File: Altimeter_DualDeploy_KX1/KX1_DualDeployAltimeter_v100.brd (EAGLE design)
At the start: 48.3 x 50.8 mm, 44 parts, among them J1 AVR_SPI_PRG_6NS, U1 ATMEGA328P, U2 BMP180, Y3 16MHz

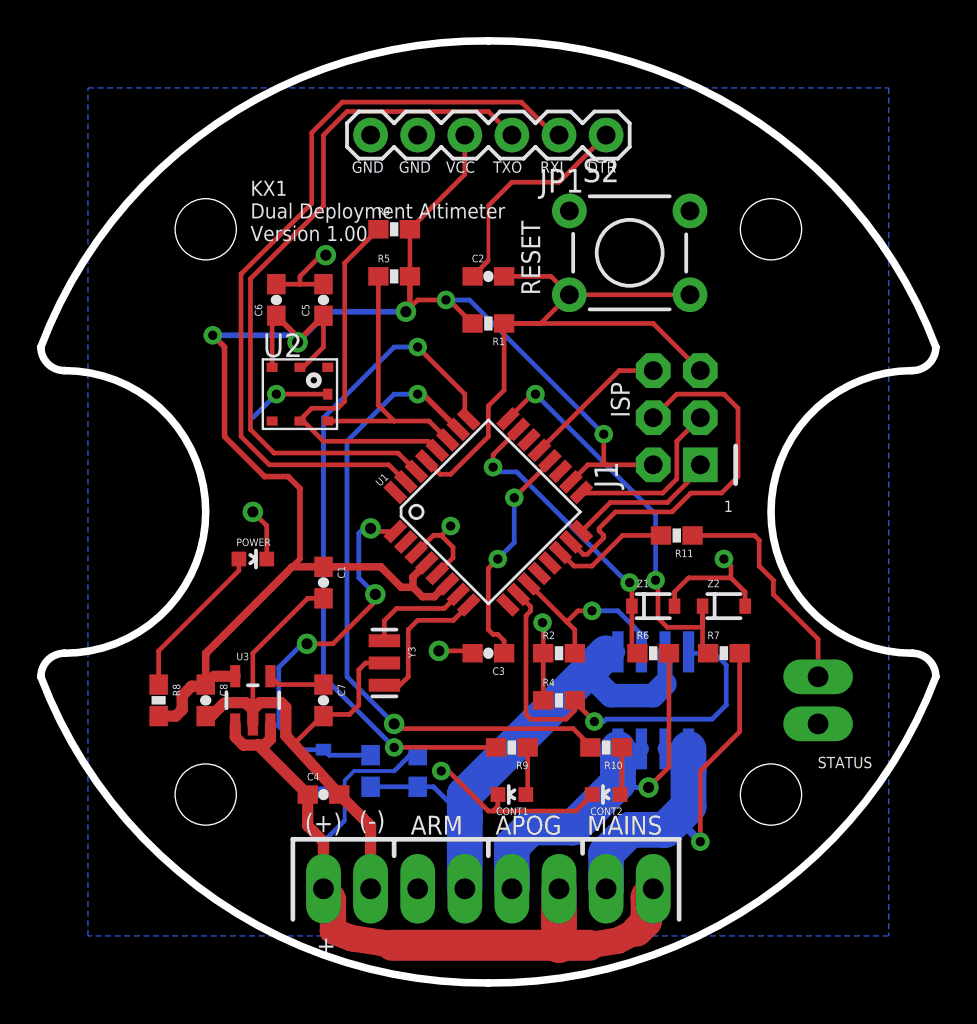
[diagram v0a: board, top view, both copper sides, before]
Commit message: Updated board layout. Tweaked silkscreen. Added V_BATT plane.
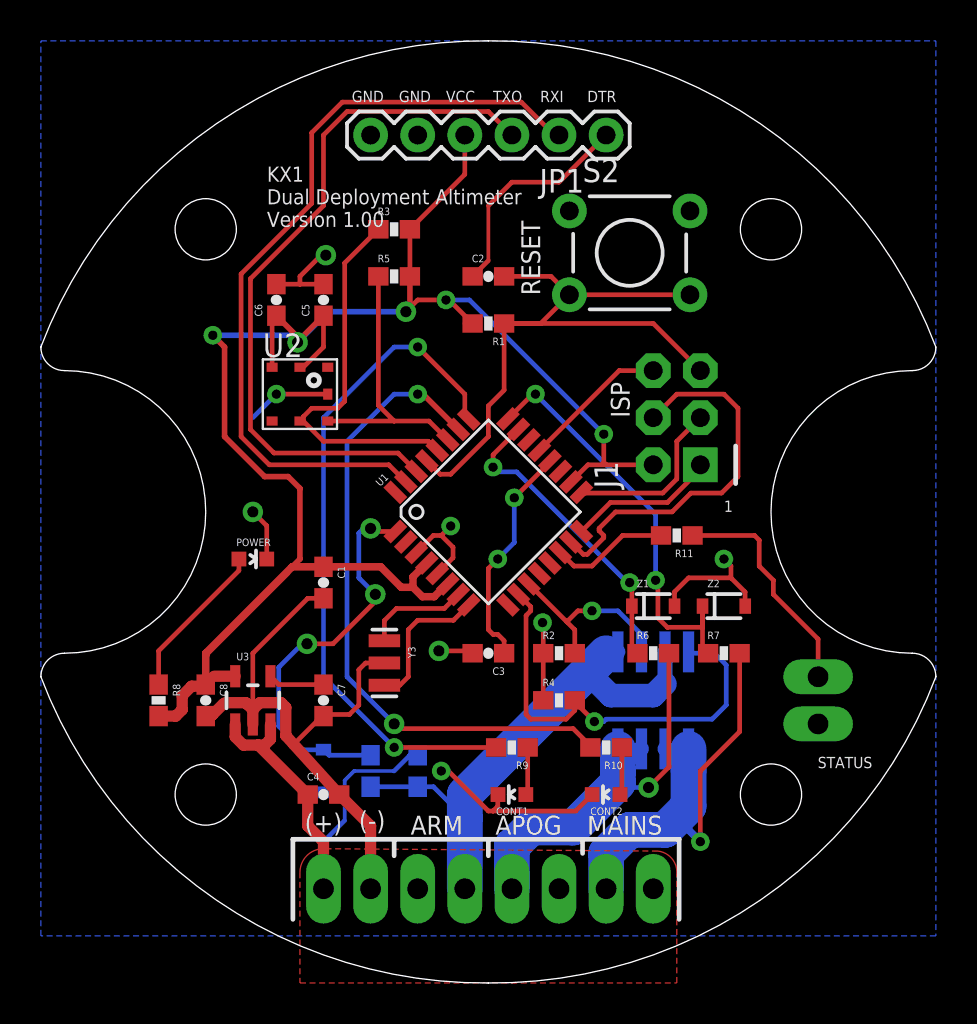
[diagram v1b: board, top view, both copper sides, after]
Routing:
- net V_BATT: track 48.5 -> 23.7 mm
- added copper zone on layer 1, net V_BATT
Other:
- board text removed: "+"
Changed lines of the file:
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@@
 <board>
 <plain>
-<wire x1="24.13" y1="50.8" x2="48.26" y2="34.29" width="0.4064" layer="20" curve="-69.775141"/>
-<wire x1="48.26" y1="34.29" x2="46.99" y2="33.02" width="0.4064" layer="20" curve="-90"/>
-<wire x1="46.99" y1="33.02" x2="46.99" y2="17.78" width="0.4064" layer="20" curve="180"/>
-<wire x1="48.26" y1="16.51" x2="46.99" y2="17.78" width="0.4064" layer="20" curve="90"/>
-<wire x1="24.13" y1="50.8" x2="0" y2="34.29" width="0.4064" layer="20" curve="69.775141"/>
-<wire x1="0" y1="34.29" x2="1.27" y2="33.02" width="0.4064" layer="20" curve="90"/>
-<wire x1="24.13" y1="0" x2="48.26" y2="16.51" width="0.4064" layer="20" curve="69.775141"/>
-<wire x1="24.13" y1="0" x2="0" y2="16.51" width="0.4064" layer="20" curve="-69.775141"/>
-<wire x1="0" y1="16.51" x2="1.27" y2="17.78" width="0.4064" layer="20" curve="-90"/>
-<wire x1="1.27" y1="33.02" x2="1.27" y2="17.78" width="0.4064" layer="20" curve="-180"/>
+<wire x1="24.13" y1="50.8" x2="48.26" y2="34.29" width="0.0508" layer="20" curve="-69.775141"/>
+<wire x1="48.26" y1="34.29" x2="46.99" y2="33.02" width="0.0508" layer="20" curve="-90"/>
+<wire x1="46.99" y1="33.02" x2="46.99" y2="17.78" width="0.0508" layer="20" curve="180"/>
+<wire x1="48.26" y1="16.51" x2="46.99" y2="17.78" width="0.0508" layer="20" curve="90"/>
+<wire x1="24.13" y1="50.8" x2="0" y2="34.29" width="0.0508" layer="20" curve="69.775141"/>
+<wire x1="0" y1="34.29" x2="1.27" y2="33.02" width="0.0508" layer="20" curve="90"/>
+<wire x1="24.13" y1="0" x2="48.26" y2="16.51" width="0.0508" layer="20" curve="69.775141"/>
+<wire x1="24.13" y1="0" x2="0" y2="16.51" width="0.0508" layer="20" curve="-69.775141"/>
+<wire x1="0" y1="16.51" x2="1.27" y2="17.78" width="0.0508" layer="20" curve="-90"/>
+<wire x1="1.27" y1="33.02" x2="1.27" y2="17.78" width="0.0508" layer="20" curve="-180"/>
 <text x="24.511" y="8.001" size="1.016" layer="21">APOG</text>
 <text x="29.464" y="8.001" size="1.016" layer="21">MAINS</text>
 <text x="36.83" y="25.4" size="0.6096" layer="21">1</text>
-<text x="16.764" y="43.688" size="0.6096" layer="21">GND</text>
-<text x="11.303" y="40.005" size="0.8128" layer="21">KX1
+<text x="16.764" y="47.498" size="0.6096" layer="21">GND</text>
+<text x="12.192" y="40.767" size="0.8128" layer="21">KX1
 Dual Deployment Altimeter
 Version 1.00
 </text>
 <text x="19.939" y="8.001" size="1.016" layer="21">ARM</text>
-<text x="14.859" y="1.524" size="1.016" layer="21">+</text>
 <text x="17.145" y="8.255" size="1.016" layer="21">(-)</text>
 <text x="14.224" y="8.128" size="1.016" layer="21">(+)</text>
@@
 <wire x1="24.13" y1="7.747" x2="24.13" y2="6.858" width="0.254" layer="21"/>
 <wire x1="29.21" y1="7.747" x2="29.21" y2="6.985" width="0.254" layer="21"/>
-<text x="19.304" y="43.688" size="0.6096" layer="21">GND</text>
-<text x="21.844" y="43.688" size="0.6096" layer="21">VCC</text>
-<text x="24.384" y="43.688" size="0.6096" layer="21">TXO</text>
-<text x="26.924" y="43.688" size="0.6096" layer="21">RXI</text>
-<text x="29.464" y="43.688" size="0.6096" layer="21">DTR</text>
+<text x="19.304" y="47.498" size="0.6096" layer="21">GND</text>
+<text x="21.844" y="47.498" size="0.6096" layer="21">VCC</text>
+<text x="24.384" y="47.498" size="0.6096" layer="21">TXO</text>
+<text x="26.924" y="47.498" size="0.6096" layer="21">RXI</text>
+<text x="29.464" y="47.498" size="0.6096" layer="21">DTR</text>
 <text x="26.924" y="37.084" size="1.016" layer="21" rot="R90">RESET</text>
 <wire x1="37.465" y1="28.956" x2="37.465" y2="26.924" width="0.254" layer="21"/>
@@
 <contactref element="U1" pad="5"/>
 <polygon width="0.254" layer="16" isolate="0.3048" thermals="no">
-<vertex x="2.54" y="2.54"/>
-<vertex x="2.54" y="48.26"/>
-<vertex x="45.72" y="48.26"/>
-<vertex x="45.72" y="2.54"/>
+<vertex x="0" y="2.54"/>
+<vertex x="0" y="50.8"/>
+<vertex x="48.26" y="50.8"/>
+<vertex x="48.26" y="2.54"/>
 </polygon>
 <contactref element="JP1" pad="GND"/>
@@
 <wire x1="16.383" y1="8.763" x2="15.24" y2="7.62" width="0.254" layer="16"/>
 <wire x1="15.24" y1="7.62" x2="15.24" y2="5.08" width="0.254" layer="16"/>
-<wire x1="33.02" y1="5.08" x2="32.71339375" y2="4.77339375" width="1.6764" layer="1"/>
-<wire x1="32.71339375" y1="4.77339375" x2="32.639" y2="4.593790625" width="1.6764" layer="1" curve="44.999295"/>
-<wire x1="32.639" y1="4.593790625" x2="32.639" y2="3.302" width="1.6764" layer="1"/>
-<wire x1="32.639" y1="3.302" x2="32.131" y2="2.794" width="1.6764" layer="1"/>
-<wire x1="32.131" y1="2.794" x2="31.115" y2="2.286" width="1.4224" layer="1"/>
-<wire x1="31.115" y1="2.286" x2="29.591" y2="2.032" width="1.4224" layer="1"/>
-<wire x1="29.591" y1="2.032" x2="27.94" y2="2.032" width="1.6764" layer="1"/>
-<wire x1="27.94" y1="2.032" x2="18.923" y2="2.032" width="1.6764" layer="1"/>
-<wire x1="18.923" y1="2.032" x2="18.415" y2="2.159" width="1.4224" layer="1"/>
-<wire x1="18.415" y1="2.159" x2="16.764" y2="2.413" width="1.4224" layer="1"/>
-<wire x1="16.764" y1="2.413" x2="15.748" y2="2.794" width="1.4224" layer="1"/>
-<wire x1="15.748" y1="2.794" x2="15.748" y2="4.466790625" width="1.4224" layer="1"/>
-<wire x1="15.748" y1="4.466790625" x2="15.67360625" y2="4.64639375" width="1.4224" layer="1" curve="44.999502"/>
-<wire x1="15.67360625" y1="4.64639375" x2="15.24" y2="5.08" width="1.4224" layer="1"/>
-<wire x1="27.94" y1="5.08" x2="27.94" y2="2.032" width="1.9304" layer="1"/>
+<polygon width="0.0508" layer="1" isolate="0.4064" thermals="no">
+<vertex x="15.24" y="7.239" curve="90"/>
+<vertex x="13.97" y="5.969"/>
+<vertex x="13.97" y="0"/>
+<vertex x="34.29" y="0"/>
+<vertex x="34.29" y="5.842" curve="90"/>
+<vertex x="33.274" y="7.112"/>
+</polygon>
 </signal>
 <signal name="DEPLOY2">
@@
 </signal>
 </signals>
+<errors>
+</errors>
 </board>
 </drawing>
